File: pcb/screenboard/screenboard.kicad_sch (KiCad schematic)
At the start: 72 parts, among them J1 0.5mm, J2 I-PEX, J3 1mm, J4 0.5mm, J5 0.5mm, U1 DS90CR286, U2 TPS65185

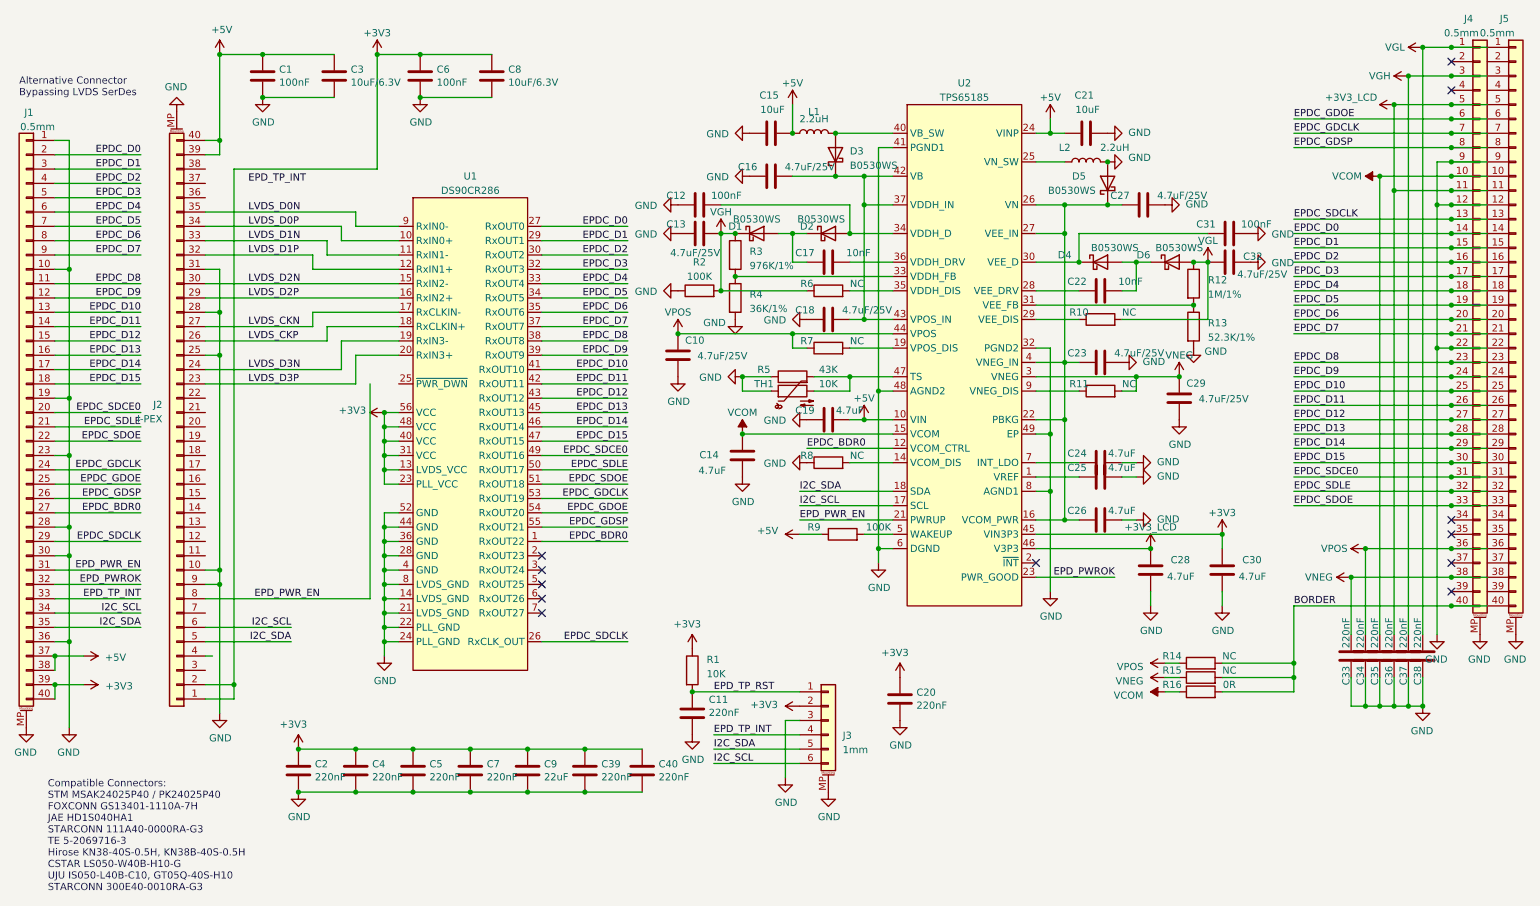
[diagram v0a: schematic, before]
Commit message: - pcb: migrate to latest kicad, r0p1
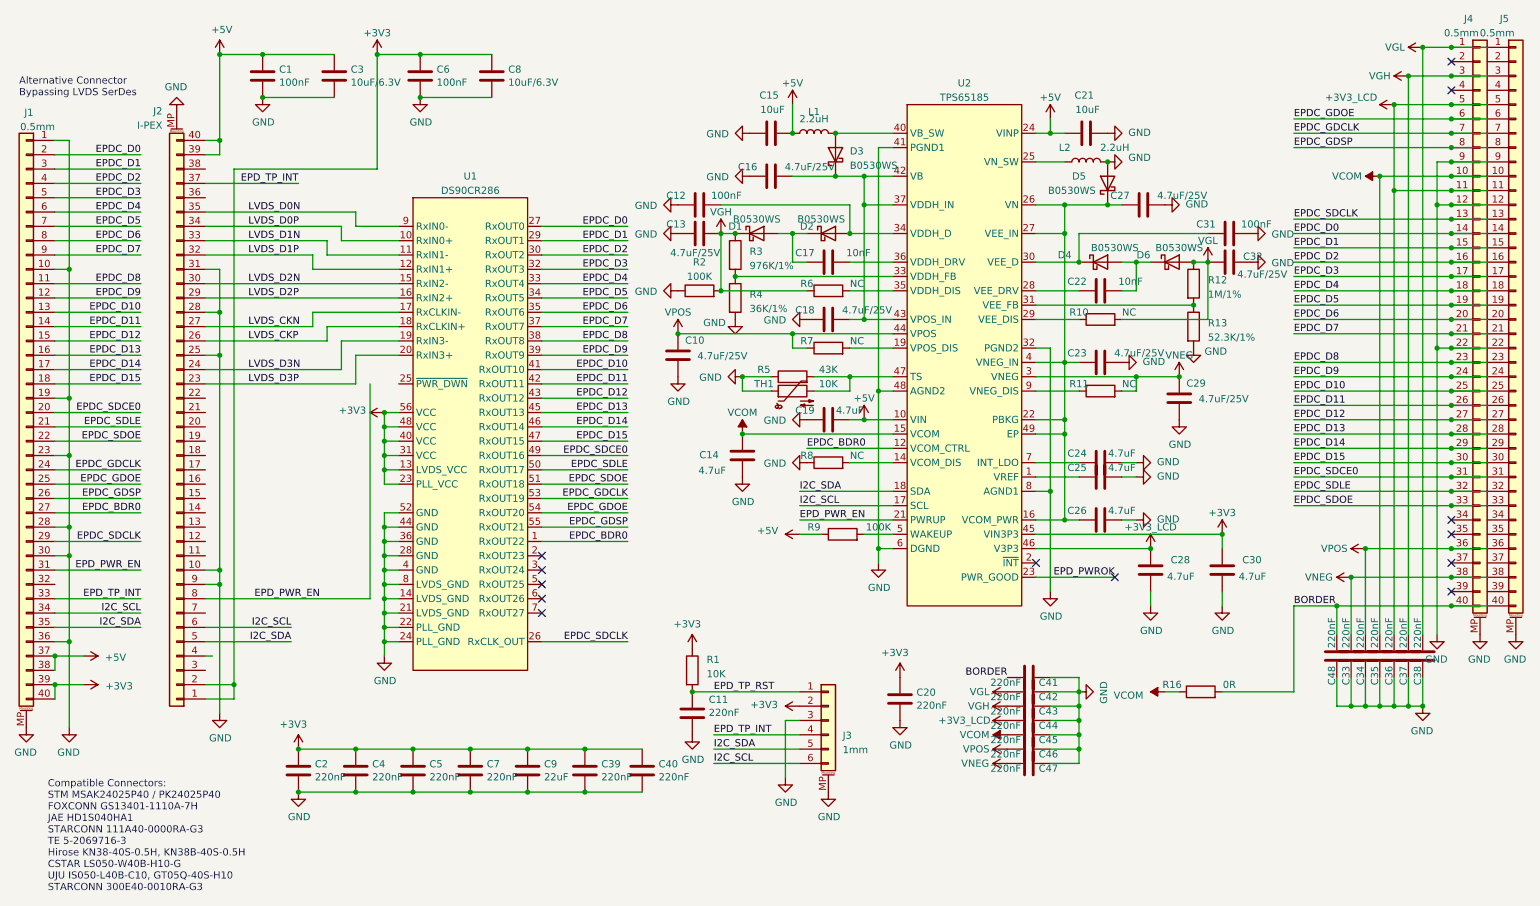
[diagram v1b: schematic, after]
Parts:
- removed R14, R15: NC, Resistor_SMD:R_0402_1005Metric, symbol Device:R
- added C41, C42, C43, C44, C45, C46, C47, C48: 220nF, Capacitor_SMD:C_0402_1005Metric, symbol Device:C
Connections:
- net +3V3_LCD: now also C44.1
- net BORDER: now also C41.1, C48.1
- net EPD_PWROK: no longer J1.32 (Pin_32)
- net EPD_TP_INT: now also J2.37 (Pin_37)
- net GND: now also C41.2, C42.2, C43.2, C44.2, C45.2, C46.2, C47.2, C48.2; no longer U2.49 (EP)
- net VCOM: now also C45.1
- net VGH: now also C43.1
- net VGL: now also C42.1
- net VNEG: now also C47.1
- net VPOS: now also C46.1
- net at C23.1, C26.1, C27.1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: now also U2.49 (EP)
- no-connect marks 12 -> 13
